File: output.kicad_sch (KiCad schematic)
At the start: 32 parts, among them J1 SMA, J2 SMA, J3 SMA, J4 SMA, J5 U.Fl, T1 MABA-007159-000000, T2 MABA-007159-000000, U6 74CB3Q3306, U7 74LVC1G125

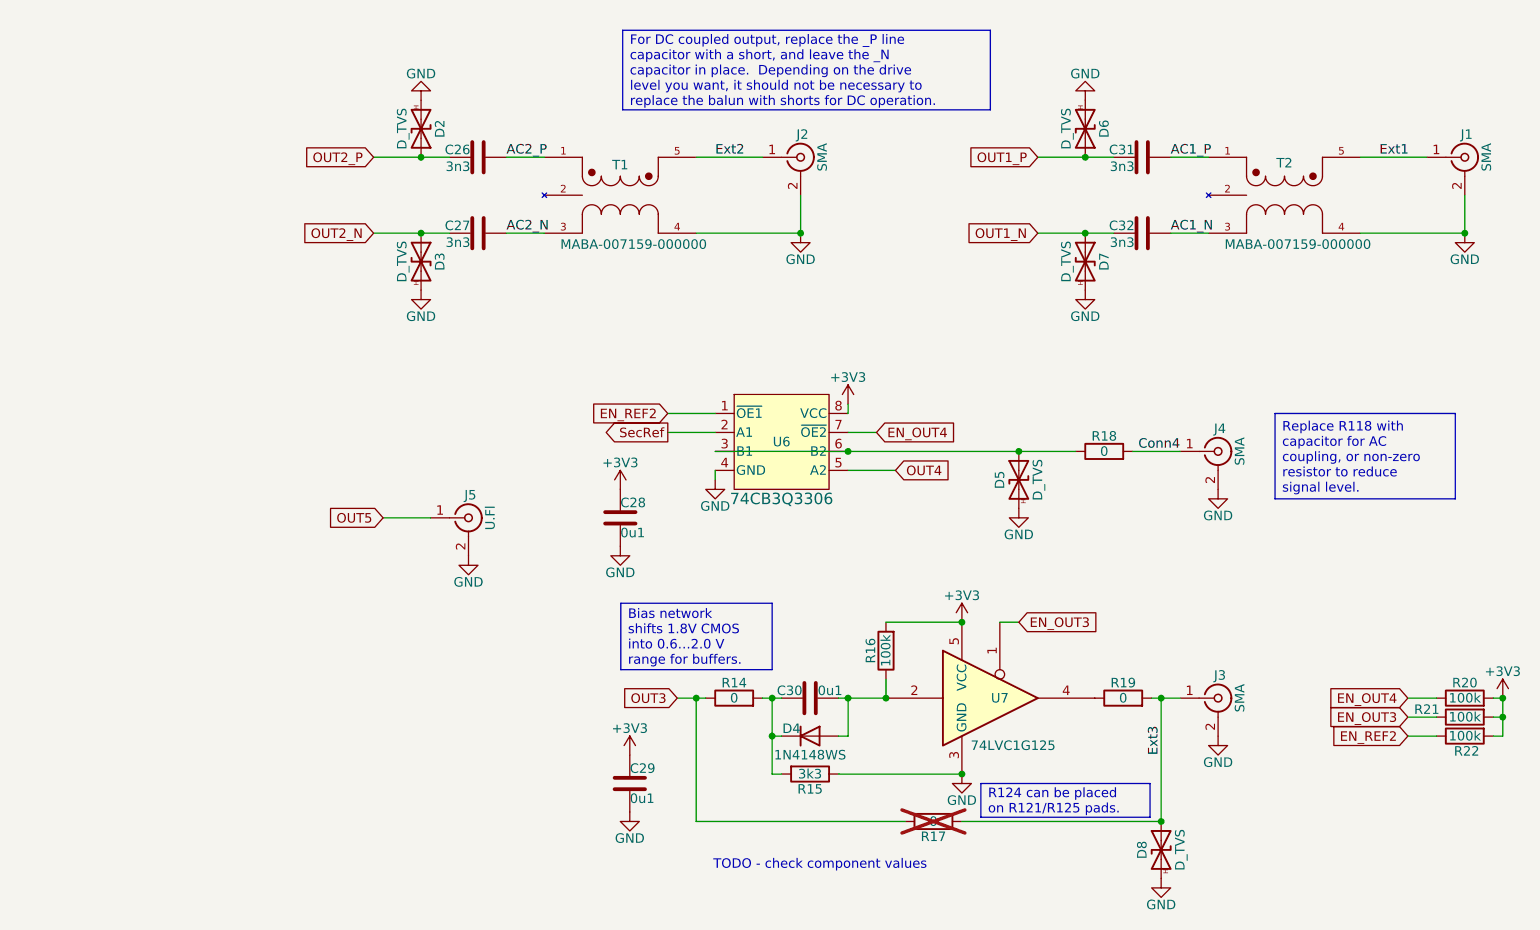
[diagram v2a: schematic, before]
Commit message: Silkscreen passes DRC.  Also we renumbered everything.
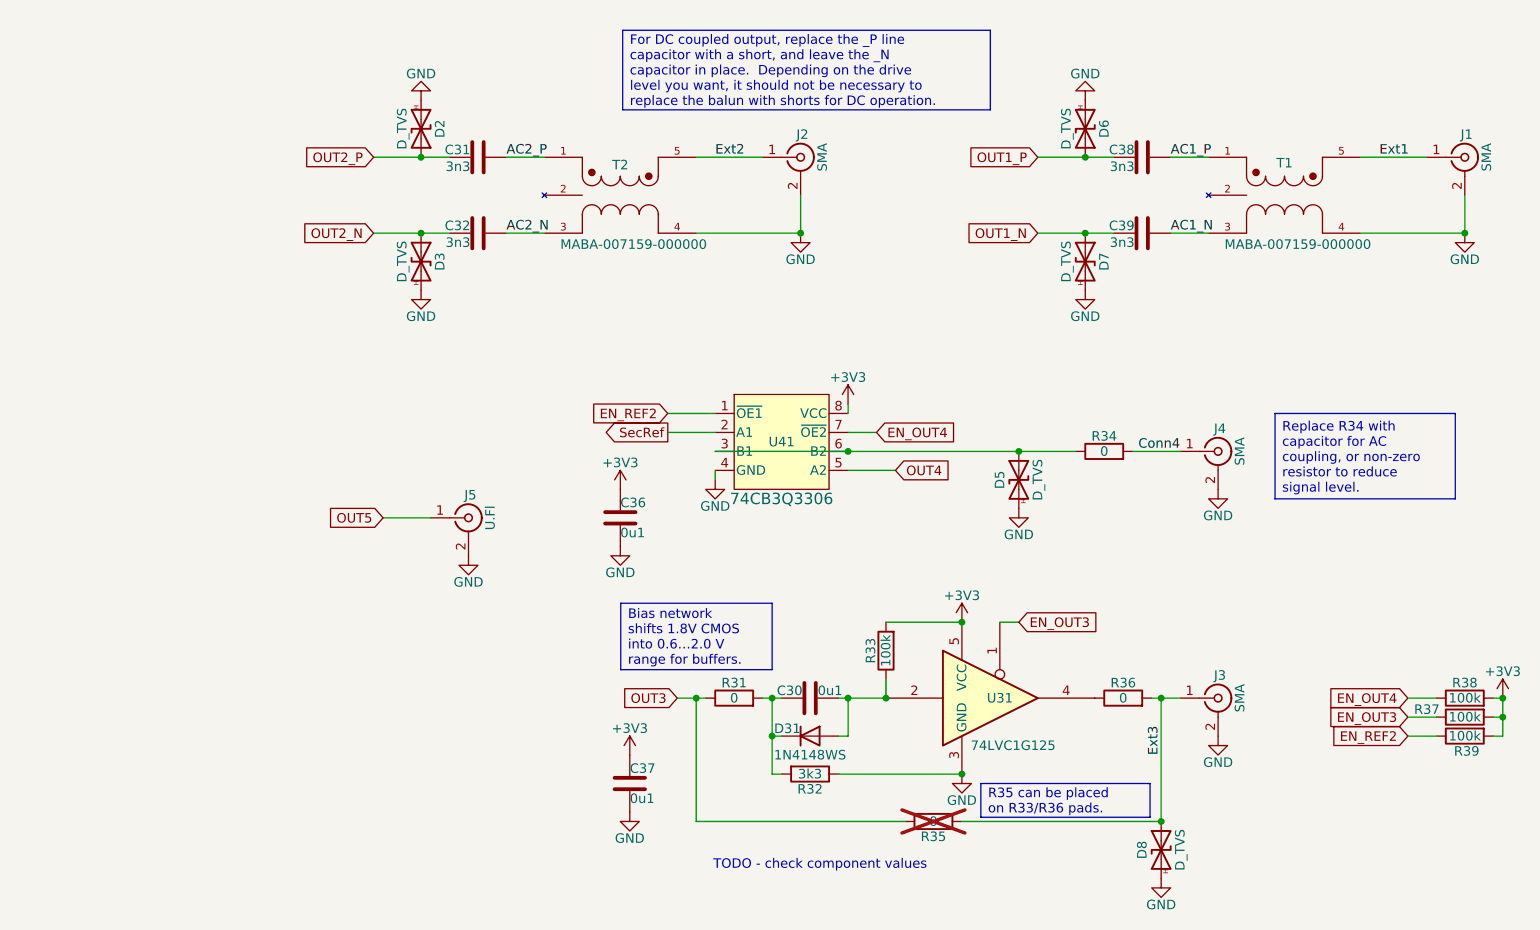
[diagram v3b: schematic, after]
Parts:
- renumbered C26 to C31, C27 to C32, C28 to C36, C29 to C37, C31 to C38, C32 to C39, D4 to D31, R14 to R31, R15 to R32, R16 to R33, R18 to R34, R17 to R35, R19 to R36, R21 to R37, R20 to R38, R22 to R39, T2 to T1, T1 to T2, U7 to U31, U6 to U41
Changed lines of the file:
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@@
 		)
 	)
-	(text_box "R124 can be placed on R121/R125 pads."
+	(text_box "R35 can be placed on R33/R36 pads."
 		(exclude_from_sim no)
 		(at 168.91 137.16 0)
@@
 		)
 	)
-	(text_box "Replace R118 with capacitor for AC coupling, or non-zero resistor to reduce signal level."
+	(text_box "Replace R34 with capacitor for AC coupling, or non-zero resistor to reduce signal level."
 		(exclude_from_sim no)
 		(at 208.28 87.63 0)
@@
 		(on_board yes)
 		(dnp no)
-		(property "Reference" "C26"
+		(property "Reference" "C31"
 			(at 100.584 53.086 90)
 			(effects
@@
 			(project "gpsref"
 				(path "/3160ff17-81c2-4674-af97-e8d9acaf6b65/26994282-45a2-461a-b033-dde2ded4d8ff"
-					(reference "C26")
+					(reference "C31")
 					(unit 1)
 				)
@@
 		(on_board yes)
 		(dnp no)
-		(property "Reference" "U6"
+		(property "Reference" "U41"
 			(at 142.24 91.44 0)
 			(effects
@@
 			(project ""
 				(path "/3160ff17-81c2-4674-af97-e8d9acaf6b65/26994282-45a2-461a-b033-dde2ded4d8ff"
-					(reference "U6")
+					(reference "U41")
 					(unit 1)
 				)
@@
 		(on_board yes)
 		(dnp no)
-		(property "Reference" "C32"
+		(property "Reference" "C39"
 			(at 189.484 63.246 90)
 			(effects
@@
 			(project "gpsref"
 				(path "/3160ff17-81c2-4674-af97-e8d9acaf6b65/26994282-45a2-461a-b033-dde2ded4d8ff"
-					(reference "C32")
+					(reference "C39")
 					(unit 1)
 				)
@@
 		(on_board yes)
 		(dnp no)
-		(property "Reference" "T2"
+		(property "Reference" "T1"
 			(at 209.5539 54.8561 0)
 			(effects
@@
 			(project "gpsref"
 				(path "/3160ff17-81c2-4674-af97-e8d9acaf6b65/26994282-45a2-461a-b033-dde2ded4d8ff"
-					(reference "T2")
+					(reference "T1")
 					(unit 1)
 				)
@@
 		(on_board no)
 		(dnp yes)
-		(property "Reference" "R17"
+		(property "Reference" "R35"
 			(at 162.56 144.272 90)
 			(effects
@@
 			(project "gpsref"
 				(path "/3160ff17-81c2-4674-af97-e8d9acaf6b65/26994282-45a2-461a-b033-dde2ded4d8ff"
-					(reference "R17")
+					(reference "R35")
 					(unit 1)
 				)
@@
 		(on_board yes)
 		(dnp no)
-		(property "Reference" "R15"
+		(property "Reference" "R32"
 			(at 146.05 137.922 90)
 			(effects
@@
 			(project "gpsref"
 				(path "/3160ff17-81c2-4674-af97-e8d9acaf6b65/26994282-45a2-461a-b033-dde2ded4d8ff"
-					(reference "R15")
+					(reference "R32")
 					(unit 1)
 				)
@@
 		(on_board yes)
 		(dnp no)
-		(property "Reference" "T1"
+		(property "Reference" "T2"
 			(at 120.6539 55.1101 0)
 			(effects
@@
 			(project ""
 				(path "/3160ff17-81c2-4674-af97-e8d9acaf6b65/26994282-45a2-461a-b033-dde2ded4d8ff"
-					(reference "T1")
+					(reference "T2")
 					(unit 1)
 				)
@@
 		(on_board yes)
 		(dnp no)
-		(property "Reference" "R22"
+		(property "Reference" "R39"
 			(at 233.934 132.842 90)
 			(effects
@@
 			(project "gpsref"
 				(path "/3160ff17-81c2-4674-af97-e8d9acaf6b65/26994282-45a2-461a-b033-dde2ded4d8ff"
-					(reference "R22")
+					(reference "R39")
 					(unit 1)
 				)
@@
 		(on_board yes)
 		(dnp no)
-		(property "Reference" "C29"
+		(property "Reference" "C37"
 			(at 121.92 135.89 0)
 			(effects
@@
 			(project "gpsref"
 				(path "/3160ff17-81c2-4674-af97-e8d9acaf6b65/26994282-45a2-461a-b033-dde2ded4d8ff"
-					(reference "C29")
+					(reference "C37")
 					(unit 1)
 				)
@@
 		(on_board yes)
 		(dnp no)
-		(property "Reference" "R19"
+		(property "Reference" "R36"
 			(at 187.96 123.698 90)
 			(effects
@@
 			(project "gpsref"
 				(path "/3160ff17-81c2-4674-af97-e8d9acaf6b65/26994282-45a2-461a-b033-dde2ded4d8ff"
-					(reference "R19")
+					(reference "R36")
 					(unit 1)
 				)
@@
 		(on_board yes)
 		(dnp no)
-		(property "Reference" "R20"
+		(property "Reference" "R38"
 			(at 233.68 123.698 90)
 			(effects
@@
 			(project "gpsref"
 				(path "/3160ff17-81c2-4674-af97-e8d9acaf6b65/26994282-45a2-461a-b033-dde2ded4d8ff"
-					(reference "R20")
+					(reference "R38")
 					(unit 1)
 				)
@@
 		(on_board yes)
 		(dnp no)
-		(property "Reference" "C27"
+		(property "Reference" "C32"
 			(at 100.584 63.246 90)
 			(effects
@@
 			(project "gpsref"
 				(path "/3160ff17-81c2-4674-af97-e8d9acaf6b65/26994282-45a2-461a-b033-dde2ded4d8ff"
-					(reference "C27")
+					(reference "C32")
 					(unit 1)
 				)
@@
 		(on_board yes)
 		(dnp no)
-		(property "Reference" "C28"
+		(property "Reference" "C36"
 			(at 120.65 100.33 0)
 			(effects
@@
 			(project "gpsref"
 				(path "/3160ff17-81c2-4674-af97-e8d9acaf6b65/26994282-45a2-461a-b033-dde2ded4d8ff"
-					(reference "C28")
+					(reference "C36")
 					(unit 1)
 				)
@@
 		(on_board yes)
 		(dnp no)
-		(property "Reference" "U7"
+		(property "Reference" "U31"
 			(at 171.45 125.73 0)
 			(effects
@@
 			(project "gpsref"
 				(path "/3160ff17-81c2-4674-af97-e8d9acaf6b65/26994282-45a2-461a-b033-dde2ded4d8ff"
-					(reference "U7")
+					(reference "U31")
 					(unit 1)
 				)
@@
 		(on_board yes)
 		(dnp no)
-		(property "Reference" "R18"
+		(property "Reference" "R34"
 			(at 185.42 90.678 90)
 			(effects
@@
 			(project "gpsref"
 				(path "/3160ff17-81c2-4674-af97-e8d9acaf6b65/26994282-45a2-461a-b033-dde2ded4d8ff"
-					(reference "R18")
+					(reference "R34")
 					(unit 1)
 				)
@@
 		(on_board yes)
 		(dnp no)
-		(property "Reference" "R14"
+		(property "Reference" "R31"
 			(at 135.89 123.698 90)
 			(effects
@@
 			(project "gpsref"
 				(path "/3160ff17-81c2-4674-af97-e8d9acaf6b65/26994282-45a2-461a-b033-dde2ded4d8ff"
-					(reference "R14")
+					(reference "R31")
 					(unit 1)
 				)
@@
 		(on_board yes)
 		(dnp no)
-		(property "Reference" "C31"
+		(property "Reference" "C38"
 			(at 189.484 53.086 90)
 			(effects
@@
 			(project "gpsref"
 				(path "/3160ff17-81c2-4674-af97-e8d9acaf6b65/26994282-45a2-461a-b033-dde2ded4d8ff"
-					(reference "C31")
+					(reference "C38")
 					(unit 1)
 				)
@@
 		(on_board yes)
 		(dnp no)
-		(property "Reference" "R16"
+		(property "Reference" "R33"
 			(at 154.178 119.38 90)
 			(effects
@@
 			(project "gpsref"
 				(path "/3160ff17-81c2-4674-af97-e8d9acaf6b65/26994282-45a2-461a-b033-dde2ded4d8ff"
-					(reference "R16")
+					(reference "R33")
 					(unit 1)
 				)
@@
 		(on_board yes)
 		(dnp no)
-		(property "Reference" "D4"
+		(property "Reference" "D31"
 			(at 144.78 130.556 0)
 			(effects
@@
 			(project ""
 				(path "/3160ff17-81c2-4674-af97-e8d9acaf6b65/26994282-45a2-461a-b033-dde2ded4d8ff"
-					(reference "D4")
+					(reference "D31")
 					(unit 1)
 				)
@@
 		(on_board yes)
 		(dnp no)
-		(property "Reference" "R21"
+		(property "Reference" "R37"
 			(at 228.6 127.254 90)
 			(effects
@@
 			(project "gpsref"
 				(path "/3160ff17-81c2-4674-af97-e8d9acaf6b65/26994282-45a2-461a-b033-dde2ded4d8ff"
-					(reference "R21")
+					(reference "R37")
 					(unit 1)
 				)

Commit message: Sorting out part number assignments.
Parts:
- C30, C36, C37: JLCPCB C307331 -> (none); LCSC (none) -> C307331
- C31, C32, C38, C39: JLCPCB C26404 -> (none); LCSC (none) -> C26404
- D31: JLCPCB C2128 -> (none); LCSC (none) -> C2128
- R31, R34, R36: JLCPCB C21189 -> (none); LCSC (none) -> C21189
- R32: JLCPCB C25890 -> (none); LCSC (none) -> C25890
- R33, R37, R38, R39: JLCPCB C25741 -> (none); LCSC (none) -> C25741
- T1, T2: JLCPCB C350943 -> (none); LCSC (none) -> C350943
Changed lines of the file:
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@@
 			)
 		)
-		(property "JLCPCB" "C307331"
-			(at 146.05 125.73 0)
+		(property "LCSC" "C307331"
+			(at 146.05 125.73 90)
 			(effects
 				(font
@@
 			)
 		)
-		(property "JLCPCB" "C26404"
-			(at 101.6 53.34 0)
+		(property "LCSC" "C26404"
+			(at 101.6 53.34 90)
 			(effects
 				(font
@@
 			)
 		)
-		(property "JLCPCB" "C26404"
-			(at 190.5 63.5 0)
+		(property "LCSC" "C26404"
+			(at 190.5 63.5 90)
 			(effects
 				(font
@@
 			)
 		)
-		(property "JLCPCB" "C350943"
+		(property "LCSC" "C350943"
 			(at 209.55 58.42 0)
 			(effects
@@
 			)
 		)
-		(property "JLCPCB" ""
-			(at 162.56 142.24 0)
-			(effects
-				(font
-					(size 1.27 1.27)
-				)
-				(hide yes)
-			)
-		)
 		(pin "2"
 		)
@@
 			)
 		)
-		(property "JLCPCB" "C25890"
-			(at 146.05 135.89 0)
+		(property "LCSC" "C25890"
+			(at 146.05 135.89 90)
 			(effects
 				(font
@@
 			)
 		)
-		(property "JLCPCB" "C350943"
+		(property "LCSC" "C350943"
 			(at 120.65 58.42 0)
 			(effects
@@
 			)
 		)
-		(property "JLCPCB" "C25741"
-			(at 233.68 130.81 0)
+		(property "LCSC" "C25741"
+			(at 233.68 130.81 90)
 			(effects
 				(font
@@
 			)
 		)
-		(property "JLCPCB" "C307331"
+		(property "LCSC" "C307331"
 			(at 121.92 137.16 0)
 			(effects
@@
 			)
 		)
-		(property "JLCPCB" "C21189"
-			(at 187.96 125.73 0)
+		(property "LCSC" "C21189"
+			(at 187.96 125.73 90)
 			(effects
 				(font
@@
 			)
 		)
-		(property "JLCPCB" "C25741"
-			(at 233.68 125.73 0)
+		(property "LCSC" "C25741"
+			(at 233.68 125.73 90)
 			(effects
 				(font
@@
 			)
 		)
-		(property "JLCPCB" "C26404"
-			(at 101.6 63.5 0)
+		(property "LCSC" "C26404"
+			(at 101.6 63.5 90)
 			(effects
 				(font
@@
 			)
 		)
-		(property "JLCPCB" "C307331"
+		(property "LCSC" "C307331"
 			(at 120.65 101.6 0)
 			(effects
@@
 			)
 		)
-		(property "JLCPCB" ""
-			(at 171.45 125.73 0)
-			(effects
-				(font
-					(size 1.27 1.27)
-				)
-				(hide yes)
-			)
-		)
 		(pin "4"
 		)
@@
 			)
 		)
-		(property "JLCPCB" "C21189"
-			(at 185.42 92.71 0)
+		(property "LCSC" "C21189"
+			(at 185.42 92.71 90)
 			(effects
 				(font
@@
 			)
 		)
-		(property "JLCPCB" ""
-			(at 100.33 101.6 0)
-			(effects
-				(font
-					(size 1.27 1.27)
-				)
-				(hide yes)
-			)
-		)
 		(pin "2"
 		)
@@
 			)
 		)
-		(property "JLCPCB" "C21189"
-			(at 135.89 125.73 0)
+		(property "LCSC" "C21189"
+			(at 135.89 125.73 90)
 			(effects
 				(font
@@
 			)
 		)
-		(property "JLCPCB" "C26404"
-			(at 190.5 53.34 0)
+		(property "LCSC" "C26404"
+			(at 190.5 53.34 90)
 			(effects
 				(font
@@
 			)
 		)
-		(property "JLCPCB" "C25741"
-			(at 156.21 119.38 0)
+		(property "LCSC" "C25741"
+			(at 156.21 119.38 90)
 			(effects
 				(font
@@
 			)
 		)
-		(property "JLCPCB" "C2128"
+		(property "LCSC" "C2128"
 			(at 146.05 130.81 0)
 			(effects
@@
 			)
 		)
-		(property "JLCPCB" "C25741"
-			(at 233.68 128.27 0)
+		(property "LCSC" "C25741"
+			(at 233.68 128.27 90)
 			(effects
 				(font

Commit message: Change the programming connector.
Change the SMA footprint to match narrow ones.
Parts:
- J1, J2, J3, J4: footprint Parts:SMA_Amphenol_132289_EdgeMount -> Parts:SMA_EdgeMount
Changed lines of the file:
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@@
 			)
 		)
-		(property "Footprint" "Parts:SMA_Amphenol_132289_EdgeMount"
+		(property "Footprint" "Parts:SMA_EdgeMount"
 			(at 200.66 125.73 0)
 			(effects
@@
 			)
 		)
-		(property "Footprint" "Parts:SMA_Amphenol_132289_EdgeMount"
+		(property "Footprint" "Parts:SMA_EdgeMount"
 			(at 200.66 92.71 0)
 			(effects
@@
 			)
 		)
-		(property "Footprint" "Parts:SMA_Amphenol_132289_EdgeMount"
+		(property "Footprint" "Parts:SMA_EdgeMount"
 			(at 144.78 53.34 0)
 			(effects
@@
 			)
 		)
-		(property "Footprint" "Parts:SMA_Amphenol_132289_EdgeMount"
+		(property "Footprint" "Parts:SMA_EdgeMount"
 			(at 233.68 53.34 0)
 			(effects

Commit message: Schematic updates for revision mostly done.
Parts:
- removed C30, C37: 0u1, Capacitor_SMD:C_0402_1005Metric, symbol Device:C
- removed D31: 1N4148WS, Diode_SMD:D_SOD-323, symbol Diode:1N4148WS
- removed R33, R37, R38, R39: 100k, Resistor_SMD:R_0402_1005Metric, symbol Device:R
- removed R34, R35, R36: 0, Resistor_SMD:R_0603_1608Metric, symbol Device:R
- removed U31: 74LVC1G125, Package_TO_SOT_SMD:SOT-23-5, symbol 74xGxx:74LVC1G125
- removed U41: 74CB3Q3306, Package_SO:VSSOP-8_2.3x2mm_P0.5mm, symbol Parts:74CB3Q3306
- added C32: 2p2, Capacitor_SMD:C_0402_1005Metric, symbol Device:C
- added C33: 100n, Capacitor_SMD:C_0402_1005Metric, symbol Device:C
- added C38: 3n3, Capacitor_SMD:C_0402_1005Metric, symbol Device:C
- added C81, C82: 10u, Capacitor_SMD:C_0402_1005Metric, symbol Device:C
- added C83, C84: 10p, Capacitor_SMD:C_0402_1005Metric, symbol Device:C
- added L31, L32: 220, Inductor_SMD:L_0603_1608Metric, symbol Parts:L_Ferrite_Power
- added U31, U32: TLV3601DCKR, Package_TO_SOT_SMD:SOT-353_SC-70-5, symbol Parts:TLV3601DCKR
- C31: renamed from C39; LCSC C26404 -> (none)
- C35: renamed from C32; LCSC C26404 -> (none)
- C36: value 0u1 -> 2p2; LCSC C307331 -> (none)
- C37: renamed from C31; value 3n3 -> 100n; LCSC C26404 -> (none)
- R31: value 0 -> 100; footprint Resistor_SMD:R_0603_1608Metric -> Resistor_SMD:R_0402_1005Metric; LCSC C21189 -> C25076
- R32: value 3k3 -> 100; LCSC C25890 -> C25076
- renumbered C38 to C34, D6 to D31, D7 to D32, D2 to D33, D3 to D34, D8 to D35, D5 to D36
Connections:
- net Conn4 is gone; now on net Ext4: J4.1 (In)
- net +3V3: now also L31.1, L32.1; no longer C36.1
- net AC1_N: now also C32.1
- net AC2_N: now also C36.1
- net Ext1: now also C34.2, C33.2; no longer T1.5
- net Ext2: now also C37.2, C38.2; no longer T2.5
- net Ext3: now also U31.1
- net GND: now also T1.1, T2.1, C32.2, C81.2, C82.2, U31.2 (V-), U32.2 (V-); no longer R32.1
- net OUT1_N: now also D31.1 (A1), C33.1; no longer C31.1, D32.1 (A1)
- net OUT1_P: now also C31.1, D32.1 (A1); no longer C34.1, D31.1 (A1)
- net at R31.2: now also C83.1; no longer R32.2
- net Ext4: now reaches D36.1 (A1)
- net Ext4: now also U32.1
- removed net AC1_P: C34.2, T1.1
- removed net AC2_P: C37.2, T2.1
- net OUT3 renamed OUT3_P
- net OUT3_P: now also U31.3 (+)
- new net: C84.1, R32.2
- new net: C34.1, T1.5
- new net: C82.1, L32.2, U32.5 (V+)
- new net: C38.1, T2.5
- new net LED_PWR: C81.1, L31.2, U31.5 (V+)
- new net OUT3_N: C83.2, U31.4 (-)
- new net OUT4_N: C84.2, U32.4 (-)
- new net OUT4_P: R32.1, U32.3 (+)
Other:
- note removed: "TODO - check component values"
- moved on the sheet: C31, C34, C35, C37, D31, D32, D33, D34, D35, D36, J1, J2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
